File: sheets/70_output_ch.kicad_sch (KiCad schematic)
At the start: 0 parts

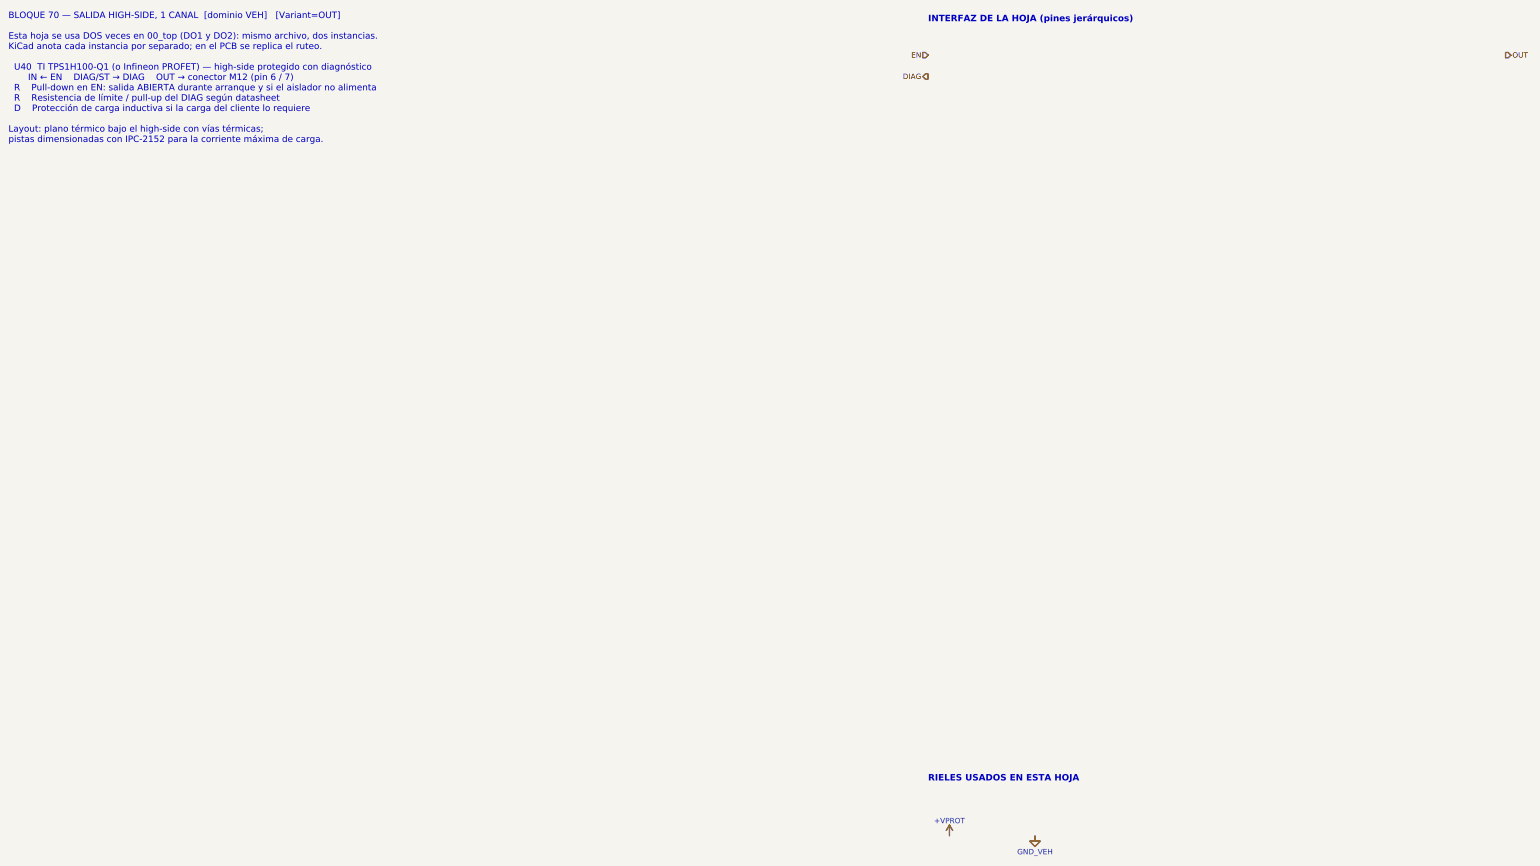
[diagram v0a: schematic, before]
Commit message: 70_output: salida low-side con latch y señal PWR_FLT
- 70_output (DO1/DO2): MOSFET FDD7N25LZ (demo, 250 V) con TVS SMCJ188A
  en el drenador, latch de sobrecorriente a ~0.7 A (R 1 ohm + BC817/BC807,
  rearme con EN=0), apagado del gate por PWR_FLT_N o latch (BAT54A) y
  DIAG por divisor del drenador con zener 5V1. OUT pasa a pasivo.
- Jerarquía: VEH_PWR_FLT_N de 10_power_input a 70_output y 20_isolation;
  PWR_FLT de 20_isolation a 40_mcu (KW45 y ESP32-S3).
- 10_power_input: solo interfaz (VEH_DO1/2 pasivos, VEH_PWR_FLT_N);
  el circuito con LM74930 va en un commit aparte.
- CLAUDE.md: procedimiento para componentes fuera de las librerías.
- README: 70_output es low-side.

Co-Authored-By: Claude Opus 5.5 <noreply@anthropic.com>
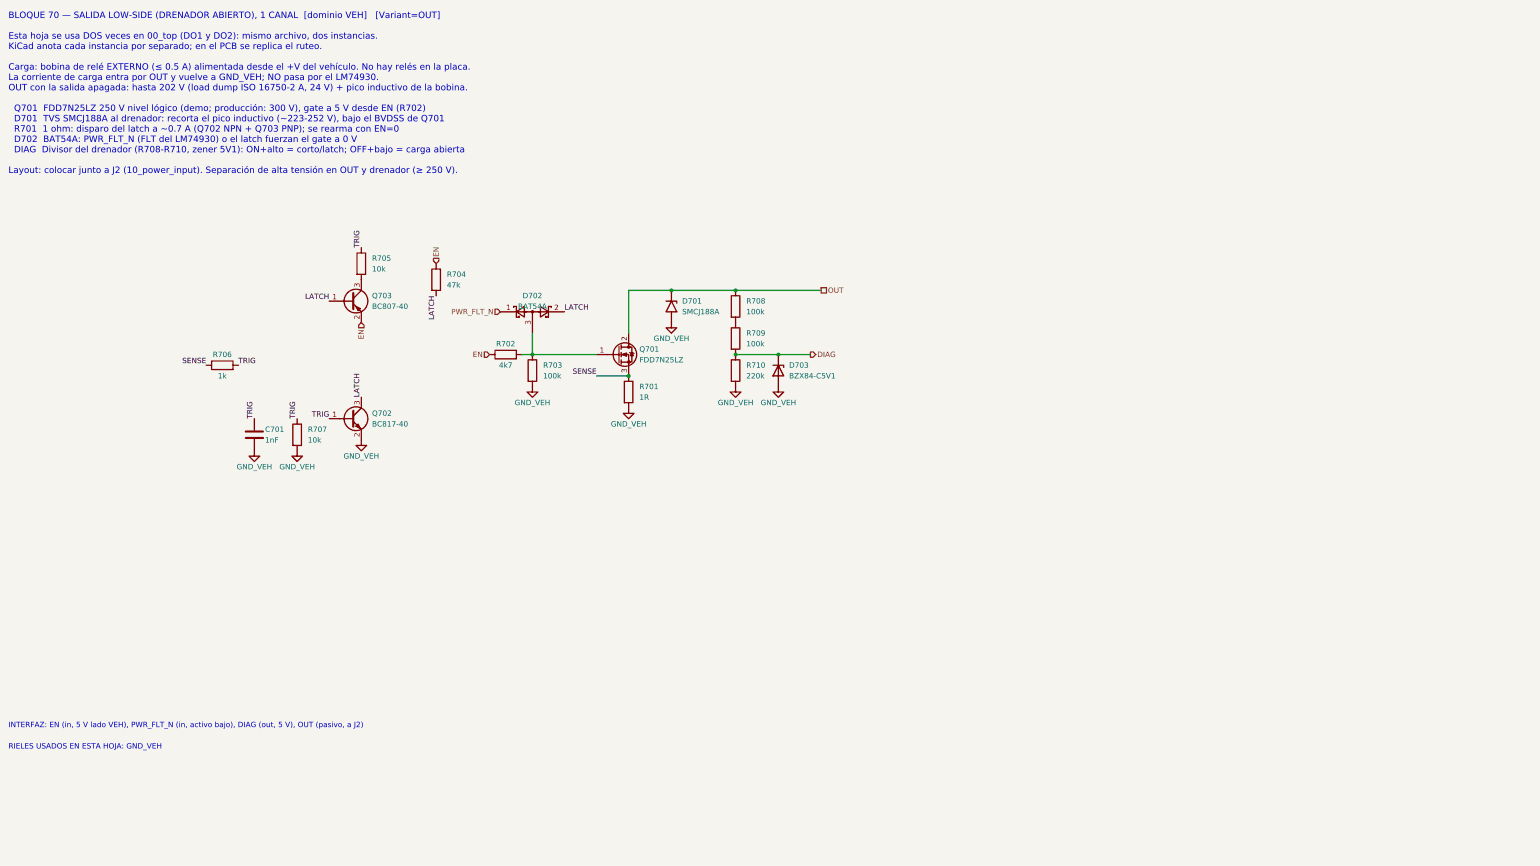
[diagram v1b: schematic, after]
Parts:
- added C701: 1nF, Capacitor_SMD:C_0603_1608Metric, symbol Device:C
- added D701: SMCJ188A, Diode_SMD:D_SMC, symbol Diode:SM6T200A
- added D702: BAT54A, Package_TO_SOT_SMD:SOT-23, symbol Diode:BAT54A
- added D703: BZX84-C5V1, Package_TO_SOT_SMD:SOT-23, symbol Diode:BZX84Cxx
- added Q701: FDD7N25LZ, Package_TO_SOT_SMD:TO-252-2, symbol Transistor_FET:IPD50R380CE
- added Q702: BC817-40, Package_TO_SOT_SMD:SOT-23, symbol Transistor_BJT:Q_NPN_BEC
- added Q703: BC807-40, Package_TO_SOT_SMD:SOT-23, symbol Transistor_BJT:Q_PNP_BEC
- added R701: 1R, Resistor_SMD:R_1206_3216Metric, symbol Device:R
- added R702: 4k7, Resistor_SMD:R_0603_1608Metric, symbol Device:R
- added R703: 100k, Resistor_SMD:R_0603_1608Metric, symbol Device:R
- added R704: 47k, Resistor_SMD:R_0603_1608Metric, symbol Device:R
- added R705, R707: 10k, Resistor_SMD:R_0603_1608Metric, symbol Device:R
- added R706: 1k, Resistor_SMD:R_0603_1608Metric, symbol Device:R
- added R708, R709: 100k, Resistor_SMD:R_1206_3216Metric, symbol Device:R
- added R710: 220k, Resistor_SMD:R_0603_1608Metric, symbol Device:R
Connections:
- net DIAG: now also D703.3 (K), R709.2, R710.1
- net EN: now also Q703.2 (E), R702.1, R704.1
- net GND_VEH: now also C701.2, D701.2 (A2), D703.1 (A), Q702.2 (E), R701.2, R703.2, R707.2, R710.2
- net OUT: now also D701.1 (A1), Q701.2 (D), R708.1
- new net: D702.3, Q701.1 (G), R702.2, R703.1
- new net: R708.2, R709.1
- new net: Q703.3 (C), R705.2
- new net LATCH: D702.2, Q702.3 (C), Q703.1 (B), R704.2
- new net PWR_FLT_N: D702.1
- new net SENSE: Q701.3 (S), R701.1, R706.1
- new net TRIG: C701.1, Q702.1 (B), R705.1, R706.2, R707.1
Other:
- note added: "BLOQUE 70 — SALIDA LOW-SIDE (DRENADOR ABIERTO), 1 CANAL [dominio VEH] [Variant=OUT] Esta hoja se usa DOS veces en 00_top (DO1 y DO2): mismo archivo, dos instancias. KiCad anota cada instancia por separado; en el PCB se replica el ruteo. Carga: bobina de relé EXTERNO (≤ 0.5 A) alimentada desde el +V del vehículo. No hay relés en la placa. La corriente de carga entra por OUT y vuelve a GND_VEH; NO 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"
- note added: "INTERFAZ: EN (in, 5 V lado VEH), PWR_FLT_N (in, activo bajo), DIAG (out, 5 V), OUT (pasivo, a J2)"
- note added: "RIELES USADOS EN ESTA HOJA: GND_VEH"
- note removed: "BLOQUE 70 — SALIDA HIGH-SIDE, 1 CANAL [dominio VEH] [Variant=OUT] Esta hoja se usa DOS veces en 00_top (DO1 y DO2): mismo archivo, dos instancias. KiCad anota cada instancia por separado; en el PCB se replica el ruteo. U40 TI TPS1H100-Q1 (o Infineon PROFET) — high-side protegido con diagnóstico IN ← EN DIAG/ST → DIAG OUT → conector M12 (pin 6 / 7) R Pull-down en EN: salida ABIERTA durante arranqu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"
- note removed: "INTERFAZ DE LA HOJA (pines jerárquicos)"
- note removed: "RIELES USADOS EN ESTA HOJA"
- title: Salida high-side (1 canal, se instancia 2 veces) -> Salida low-side drenador abierto (x2)

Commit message: Nota EP/RTN de U101, regla de PCB y verificación del FDD7N25LZ
- 10_power_input: nota visible junto a U101 "EP/RTN flotante: NO conectar
  a GND (datasheet SNOSDF6, tabla 5-1 y sección 8.3)".
- CLAUDE.md (PCB): la red del pad 25 de U101 nunca se une a GND ni a otra
  red; regla DRC personalizada al empezar el PCB.
- 70_output: Notes de Q701 con datos del datasheet: no es AEC-Q101,
  RDS(on) a 5 V (0.57 ohm máx a 25 C, ~0.91 ohm a 85 C), margen de BVDSS
  y SOA con corto a +32 V. El filtro del latch no necesita cambios.
- docs/datasheets/FDD7N25LZ.pdf.

Co-Authored-By: Claude Opus 5.5 <noreply@anthropic.com>
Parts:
- Q701: Notes DEMO: 250 V nivel logico. Con D701 SMCJ188A el margen a 85 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 -> DEMO, NO es AEC-Q101 (el datasheet onsemi/Fairchild Rev 1.5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
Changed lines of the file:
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@@
 			)
 		)
-		(property "Notes" "DEMO: 250 V nivel logico. Con D701 SMCJ188A el margen a 85 C es ~13 V (recorte ~252 V vs BVDSS min ~265 V). PRODUCCION: buscar MOSFET de 300 V. PENDIENTE: confirmar RDS(on) a 5 V y grado automotriz en el datasheet."
+		(property "Notes" "DEMO, NO es AEC-Q101 (el datasheet onsemi/Fairchild Rev 1.5 no lo indica). PRODUCCION: buscar MOSFET de 300 V. RDS(on) a VGS=5 V: 0.45 typ / 0.57 max ohm a 25 C (ID 3.1 A); a 85 C x1.6 (Fig. 8) = ~0.72 typ / ~0.91 max ohm. Margen a 85 C contra D701 SMCJ188A (recorte ~252 V): estimado ~13 V; con Fig. 7 (BVDSS x1.07 = >=267 V) son ~15 V. SOA (Fig. 9): corto a +32 V = ~2 A (autolimitado por R701) durante <=3 us hasta que dispara el latch, muy dentro de la recta de 30 us."
 			(at 165.1 101.6 0)
 			(hide yes)
